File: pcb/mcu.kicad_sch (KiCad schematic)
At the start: 28 parts, among them J1 CON_SAMTEC_14P_2R_1m27_P_KEY_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, U3 IC_MCU_STM32F100C4T6B_48LQFP, X1 XTAL_8M_20PPM_18pF_ECS-80-18-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, X2 XTAL_32K768_10PPM_7pF_ECS-.32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

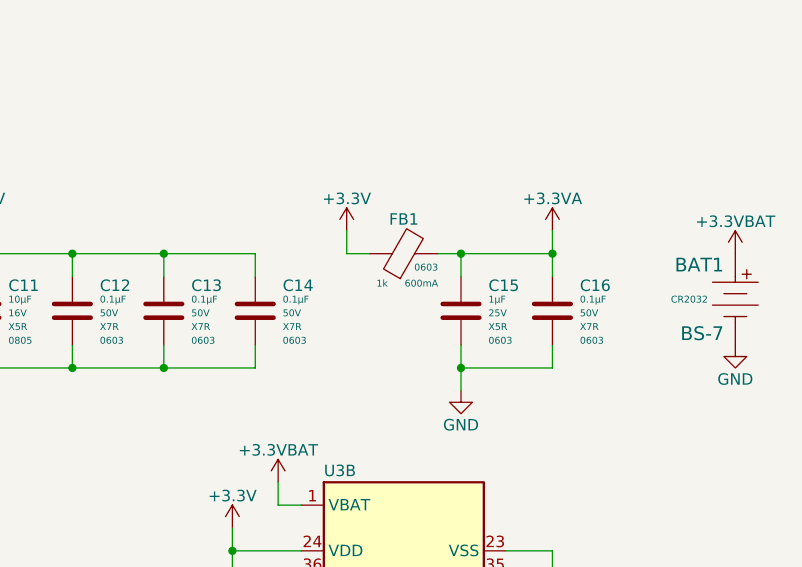
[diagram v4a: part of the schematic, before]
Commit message: Finished 12V boost circuit and updated sim to match
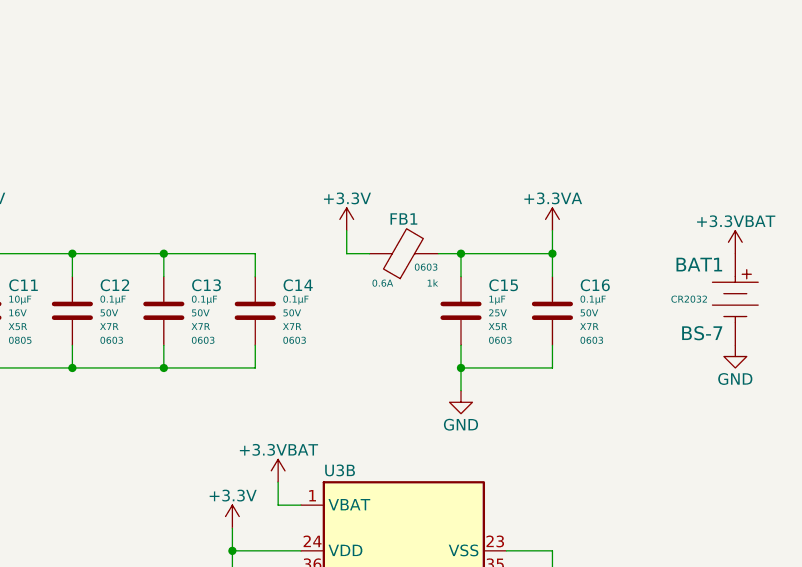
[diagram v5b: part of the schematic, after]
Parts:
- removed FB1: FER_1K_600mA_0603, Inductor_SMD:L_0603_1608Metric, symbol arjun_symbols:FER_1K_600mA_0603
- added FB1: FER_1K_0A6_0603, Inductor_SMD:L_0603_1608Metric, symbol .arjun:FER_1K_0A6_0603
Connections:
- net +3.3V: now also FB1.1
- net +3.3VA: now also FB1.2
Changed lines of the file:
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@@
+    (pin "2")
+  )
+  (symbol (lib_id ".arjun:FER_1K_0A6_0603") (at 233.68 104.14 0) (unit 1)
+    (in_bom yes) (on_board yes)
+    (property "Reference" "FB1" (id 0) (at 237.49 100.33 0))
+    (property "Value" "FER_1K_0A6_0603" (id 1) (at 263.525 97.79 0)
+      (effects (font (size 1.27 1.27)) hide)
+    )
+    (property "Footprint" "Inductor_SMD:L_0603_1608Metric" (id 2) (at 261.874 95.25 0)
+      (effects (font (size 1.27 1.27)) hide)
+    )
+    (property "Datasheet" "https://www.we-online.com/components/products/datasheet/742792662.pdf" (id 3) (at 291.465 110.49 0)
+      (effects (font (size 1.27 1.27)) hide)
+    )
+    (property "Manufacturer" "Würth Elektronik" (id 4) (at 253.365 100.33 0)
+      (effects (font (size 1.27 1.27)) (justify left) hide)
+    )
+    (property "ManufacturerPN" "742792662" (id 5) (at 253.365 102.87 0)
+      (effects (font (size 1.27 1.27)) (justify left) hide)
+    )
+    (property "Vendor" "Digi-Key" (id 6) (at 253.365 105.41 0)
+      (effects (font (size 1.27 1.27)) (justify left) hide)
+    )
+    (property "VendorPN" "732-4670-1-ND" (id 7) (at 253.365 107.95 0)
+      (effects (font (size 1.27 1.27)) (justify left) hide)
+    )
+    (property "Impedance@100MHz" "1k" (id 8) (at 241.3 107.442 0)
+      (effects (font (size 0.762 0.762)) (justify right))
+    )
+    (property "Rated Current" "0.6A" (id 9) (at 233.934 107.442 0)
+      (effects (font (size 0.762 0.762)) (justify left))
+    )
+    (property "Package" "0603" (id 10) (at 241.3 105.664 0)
+      (effects (font (size 0.762 0.762)) (justify right))
+    )
+    (pin "1")
     (pin "2")
   )
@@
     (pin "4")
   )
-  (symbol (lib_id "arjun_symbols:FER_1K_600mA_0603") (at 233.68 104.14 0) (unit 1)
-    (in_bom yes) (on_board yes)
-    (property "Reference" "FB1" (id 0) (at 237.49 100.33 0))
-    (property "Value" "FER_1K_600mA_0603" (id 1) (at 263.525 97.79 0)
-      (effects (font (size 1.27 1.27)) hide)
-    )
-    (property "Footprint" "Inductor_SMD:L_0603_1608Metric" (id 2) (at 261.874 95.25 0)
-      (effects (font (size 1.27 1.27)) hide)
-    )
-    (property "Datasheet" "https://www.we-online.com/components/products/datasheet/742792662.pdf" (id 3) (at 291.465 110.49 0)
-      (effects (font (size 1.27 1.27)) hide)
-    )
-    (property "Manufacturer" "Würth Elektronik" (id 4) (at 253.365 100.33 0)
-      (effects (font (size 1.27 1.27)) (justify left) hide)
-    )
-    (property "ManufacturerPN" "742792662" (id 5) (at 253.365 102.87 0)
-      (effects (font (size 1.27 1.27)) (justify left) hide)
-    )
-    (property "Vendor" "Digi-Key" (id 6) (at 253.365 105.41 0)
-      (effects (font (size 1.27 1.27)) (justify left) hide)
-    )
-    (property "VendorPN" "732-4670-1-ND" (id 7) (at 253.365 107.95 0)
-      (effects (font (size 1.27 1.27)) (justify left) hide)
-    )
-    (property "Impedance@100MHz" "1k" (id 8) (at 234.442 107.442 0)
-      (effects (font (size 0.762 0.762)) (justify left))
-    )
-    (property "Rated Current" "600mA" (id 9) (at 241.3 107.442 0)
-      (effects (font (size 0.762 0.762)) (justify right))
-    )
-    (property "Package" "0603" (id 10) (at 241.3 105.664 0)
-      (effects (font (size 0.762 0.762)) (justify right))
-    )
-    (pin "1")
-    (pin "2")
-  )
   (symbol (lib_id "power:+3.3V") (at 218.44 134.62 0) (unit 1)

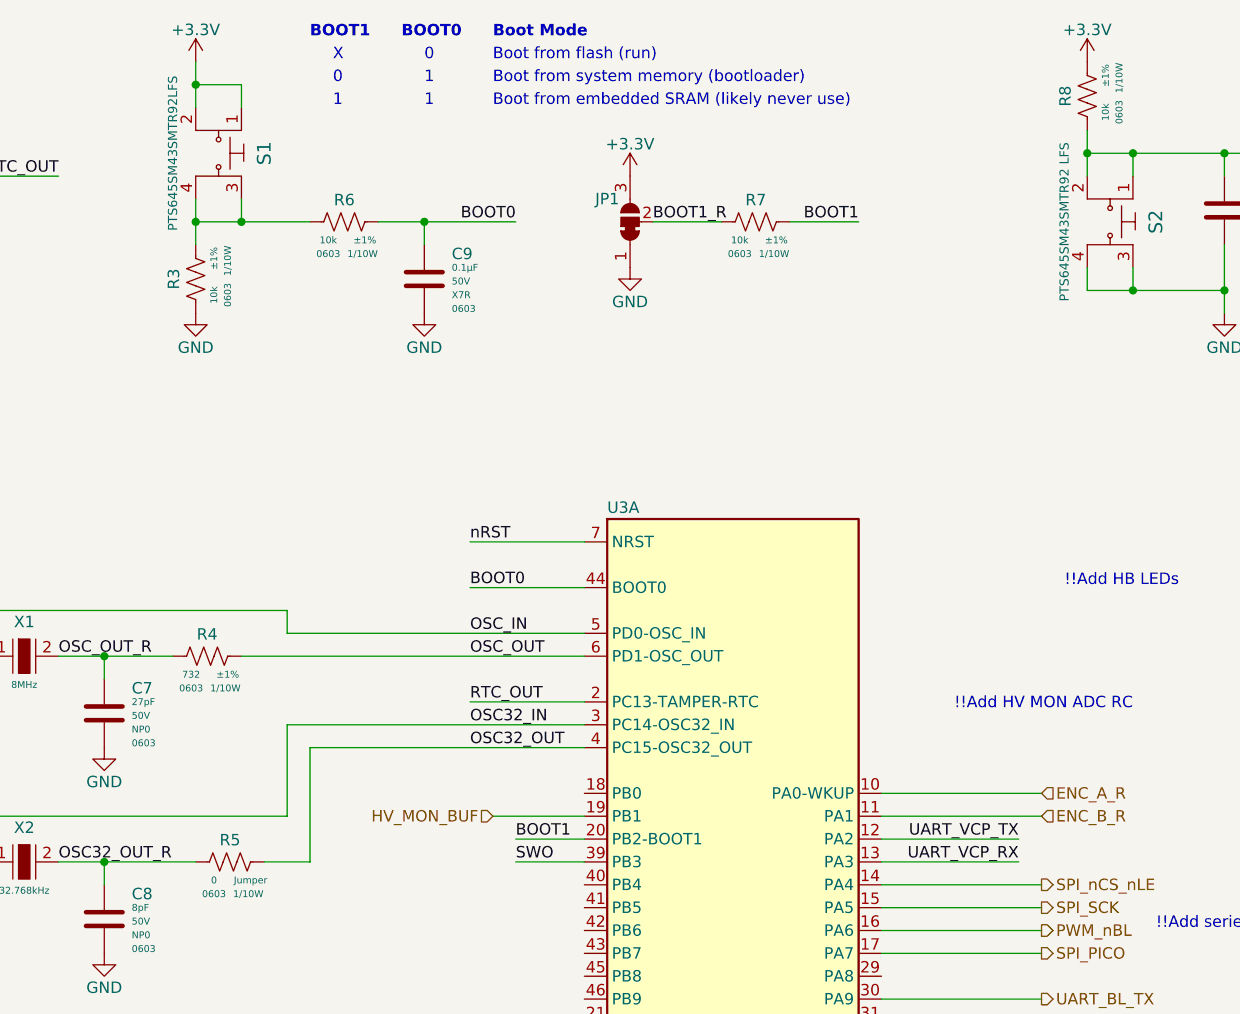
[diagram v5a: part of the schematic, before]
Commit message: Added snubber DNP footprints and named nets on power page.
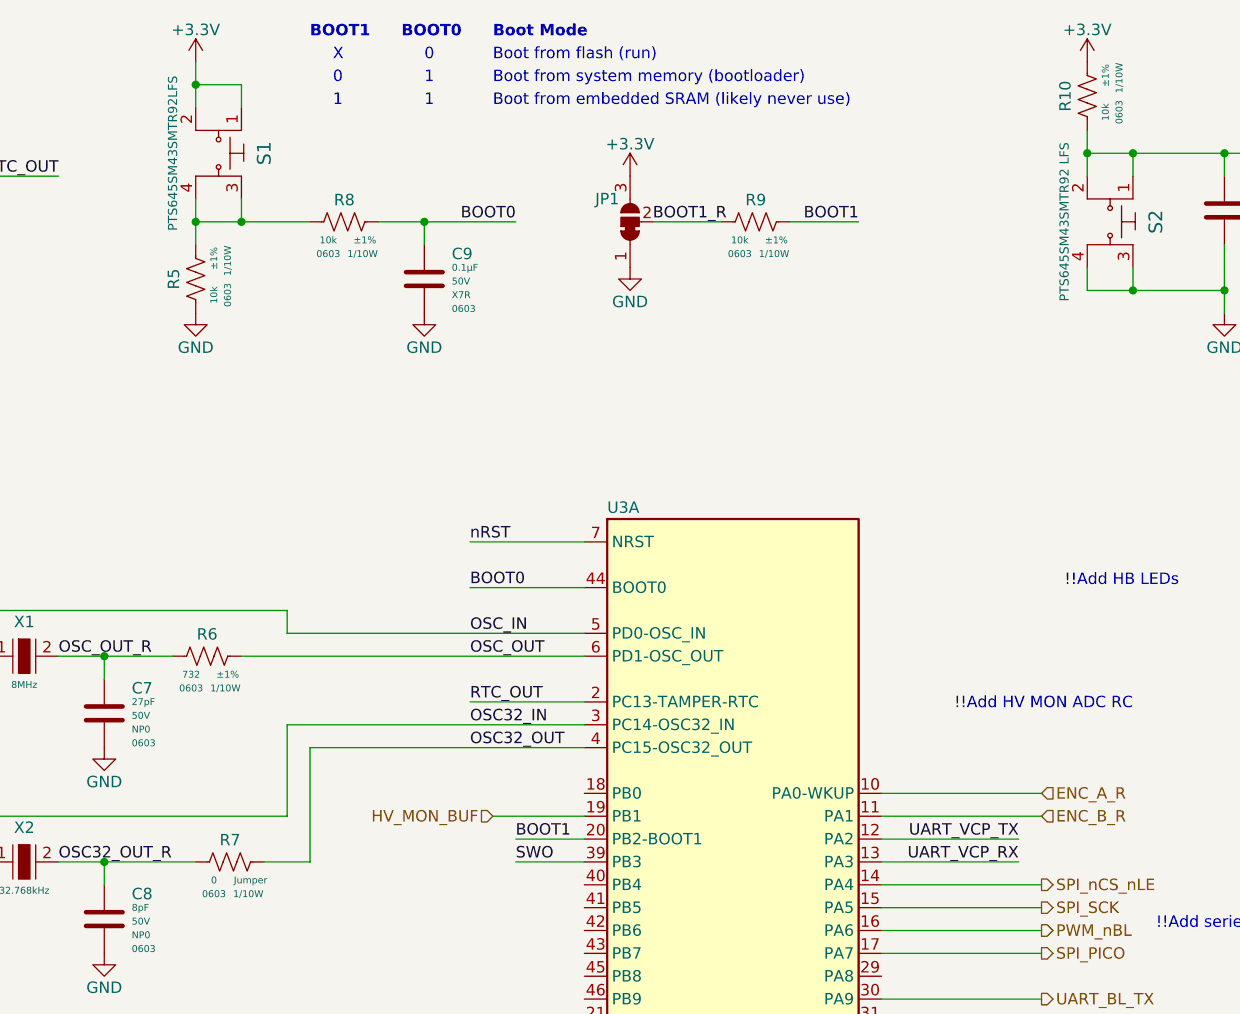
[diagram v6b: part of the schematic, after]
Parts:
- renumbered R8 to R10, R3 to R5, R4 to R6, R5 to R7, R6 to R8, R7 to R9
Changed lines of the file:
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@@
   (symbol (lib_id "power:GND") (at 243.84 119.38 0) (unit 1)
     (in_bom yes) (on_board yes)
-    (property "Reference" "#PWR026" (id 0) (at 243.84 125.73 0)
+    (property "Reference" "#PWR027" (id 0) (at 243.84 125.73 0)
       (effects (font (size 1.27 1.27)) hide)
     )
@@
   (symbol (lib_id "power:GND") (at 48.26 106.68 0) (unit 1)
     (in_bom yes) (on_board yes)
-    (property "Reference" "#PWR011" (id 0) (at 48.26 113.03 0)
+    (property "Reference" "#PWR012" (id 0) (at 48.26 113.03 0)
       (effects (font (size 1.27 1.27)) hide)
     )
@@
   (symbol (lib_id "arjun_symbols:+3.3VBAT") (at 274.32 104.14 0) (unit 1)
     (in_bom yes) (on_board yes)
-    (property "Reference" "#PWR029" (id 0) (at 274.32 107.95 0)
+    (property "Reference" "#PWR030" (id 0) (at 274.32 107.95 0)
       (effects (font (size 1.27 1.27)) hide)
     )
@@
   (symbol (lib_id "power:GND") (at 27.94 129.54 0) (unit 1)
     (in_bom yes) (on_board yes)
-    (property "Reference" "#PWR08" (id 0) (at 27.94 135.89 0)
+    (property "Reference" "#PWR09" (id 0) (at 27.94 135.89 0)
       (effects (font (size 1.27 1.27)) hide)
     )
@@
   (symbol (lib_id "power:GND") (at 58.42 58.42 0) (unit 1)
     (in_bom yes) (on_board yes)
-    (property "Reference" "#PWR014" (id 0) (at 58.42 64.77 0)
+    (property "Reference" "#PWR015" (id 0) (at 58.42 64.77 0)
       (effects (font (size 1.27 1.27)) hide)
     )
@@
   (symbol (lib_id "arjun_symbols:RES_10K_1P_1{slash}10W_0603") (at 78.74 48.26 270) (unit 1)
     (in_bom yes) (on_board yes)
-    (property "Reference" "R6" (id 0) (at 74.93 45.085 90)
+    (property "Reference" "R8" (id 0) (at 74.93 45.085 90)
       (effects (font (size 1.27 1.27)) (justify top))
     )
@@
   (symbol (lib_id "power:GND") (at 48.26 129.54 0) (unit 1)
     (in_bom yes) (on_board yes)
-    (property "Reference" "#PWR012" (id 0) (at 48.26 135.89 0)
+    (property "Reference" "#PWR013" (id 0) (at 48.26 135.89 0)
       (effects (font (size 1.27 1.27)) hide)
     )
@@
   (symbol (lib_id "arjun_symbols:RES_10K_1P_1{slash}10W_0603") (at 124.46 48.26 270) (unit 1)
     (in_bom yes) (on_board yes)
-    (property "Reference" "R7" (id 0) (at 120.65 45.085 90)
+    (property "Reference" "R9" (id 0) (at 120.65 45.085 90)
       (effects (font (size 1.27 1.27)) (justify top))
     )
@@
   (symbol (lib_id "power:+3.3V") (at 157.48 30.48 0) (unit 1)
     (in_bom yes) (on_board yes)
-    (property "Reference" "#PWR018" (id 0) (at 157.48 34.29 0)
+    (property "Reference" "#PWR019" (id 0) (at 157.48 34.29 0)
       (effects (font (size 1.27 1.27)) hide)
     )
@@
   (symbol (lib_id "power:GND") (at 172.72 58.42 0) (unit 1)
     (in_bom yes) (on_board yes)
-    (property "Reference" "#PWR019" (id 0) (at 172.72 64.77 0)
+    (property "Reference" "#PWR020" (id 0) (at 172.72 64.77 0)
       (effects (font (size 1.27 1.27)) hide)
     )
@@
   (symbol (lib_id "power:GND") (at 190.5 119.38 0) (unit 1)
     (in_bom yes) (on_board yes)
-    (property "Reference" "#PWR021" (id 0) (at 190.5 125.73 0)
+    (property "Reference" "#PWR022" (id 0) (at 190.5 125.73 0)
       (effects (font (size 1.27 1.27)) hide)
     )
@@
   (symbol (lib_id "power:GND") (at 274.32 114.3 0) (unit 1)
     (in_bom yes) (on_board yes)
-    (property "Reference" "#PWR030" (id 0) (at 274.32 120.65 0)
+    (property "Reference" "#PWR031" (id 0) (at 274.32 120.65 0)
       (effects (font (size 1.27 1.27)) hide)
     )
@@
   (symbol (lib_id "arjun_symbols:RES_10K_1P_1{slash}10W_0603") (at 58.42 50.8 0) (unit 1)
     (in_bom yes) (on_board yes)
-    (property "Reference" "R3" (id 0) (at 55.245 54.61 90)
+    (property "Reference" "R5" (id 0) (at 55.245 54.61 90)
       (effects (font (size 1.27 1.27)) (justify top))
     )
@@
   (symbol (lib_id "arjun_symbols:RES_10K_1P_1{slash}10W_0603") (at 157.48 30.48 0) (unit 1)
     (in_bom yes) (on_board yes)
-    (property "Reference" "R8" (id 0) (at 154.305 34.29 90)
+    (property "Reference" "R10" (id 0) (at 154.305 34.29 90)
       (effects (font (size 1.27 1.27)) (justify top))
     )
@@
   (symbol (lib_id "power:+3.3V") (at 190.5 101.6 0) (unit 1)
     (in_bom yes) (on_board yes)
-    (property "Reference" "#PWR020" (id 0) (at 190.5 105.41 0)
+    (property "Reference" "#PWR021" (id 0) (at 190.5 105.41 0)
       (effects (font (size 1.27 1.27)) hide)
     )
@@
   (symbol (lib_id "power:GND") (at 83.82 58.42 0) (unit 1)
     (in_bom yes) (on_board yes)
-    (property "Reference" "#PWR015" (id 0) (at 83.82 64.77 0)
+    (property "Reference" "#PWR016" (id 0) (at 83.82 64.77 0)
       (effects (font (size 1.27 1.27)) hide)
     )
@@
   (symbol (lib_id "power:+3.3V") (at 106.68 43.18 0) (unit 1)
     (in_bom yes) (on_board yes)
-    (property "Reference" "#PWR016" (id 0) (at 106.68 46.99 0)
+    (property "Reference" "#PWR017" (id 0) (at 106.68 46.99 0)
       (effects (font (size 1.27 1.27)) hide)
     )
@@
   (symbol (lib_id "arjun_symbols:RES_732R_1P_1{slash}10W_0603") (at 63.5 96.52 270) (unit 1)
     (in_bom yes) (on_board yes)
-    (property "Reference" "R4" (id 0) (at 59.69 93.345 90)
+    (property "Reference" "R6" (id 0) (at 59.69 93.345 90)
       (effects (font (size 1.27 1.27)) (justify top))
     )
@@
   (symbol (lib_id "power:+3.3V") (at 231.14 101.6 0) (unit 1)
     (in_bom yes) (on_board yes)
-    (property "Reference" "#PWR025" (id 0) (at 231.14 105.41 0)
+    (property "Reference" "#PWR026" (id 0) (at 231.14 105.41 0)
       (effects (font (size 1.27 1.27)) hide)
     )
@@
   (symbol (lib_id "power:+3.3VA") (at 254 101.6 0) (unit 1)
     (in_bom yes) (on_board yes)
-    (property "Reference" "#PWR027" (id 0) (at 254 105.41 0)
+    (property "Reference" "#PWR028" (id 0) (at 254 105.41 0)
       (effects (font (size 1.27 1.27)) hide)
     )
@@
   (symbol (lib_id "power:+3.3V") (at 38.1 160.02 0) (unit 1)
     (in_bom yes) (on_board yes)
-    (property "Reference" "#PWR010" (id 0) (at 38.1 163.83 0)
+    (property "Reference" "#PWR011" (id 0) (at 38.1 163.83 0)
       (effects (font (size 1.27 1.27)) hide)
     )
@@
   (symbol (lib_id "power:+3.3VA") (at 213.36 144.78 0) (unit 1)
     (in_bom yes) (on_board yes)
-    (property "Reference" "#PWR022" (id 0) (at 213.36 148.59 0)
+    (property "Reference" "#PWR023" (id 0) (at 213.36 148.59 0)
       (effects (font (size 1.27 1.27)) hide)
     )
@@
   (symbol (lib_id "arjun_symbols:+3.3VBAT") (at 223.52 129.54 0) (unit 1)
     (in_bom yes) (on_board yes)
-    (property "Reference" "#PWR024" (id 0) (at 223.52 133.35 0)
+    (property "Reference" "#PWR025" (id 0) (at 223.52 133.35 0)
       (effects (font (size 1.27 1.27)) hide)
     )
@@
   (symbol (lib_id "power:GND") (at 27.94 177.8 0) (unit 1)
     (in_bom yes) (on_board yes)
-    (property "Reference" "#PWR09" (id 0) (at 27.94 184.15 0)
+    (property "Reference" "#PWR010" (id 0) (at 27.94 184.15 0)
       (effects (font (size 1.27 1.27)) hide)
     )
@@
   (symbol (lib_id "power:GND") (at 254 149.86 0) (unit 1)
     (in_bom yes) (on_board yes)
-    (property "Reference" "#PWR028" (id 0) (at 254 156.21 0)
+    (property "Reference" "#PWR029" (id 0) (at 254 156.21 0)
       (effects (font (size 1.27 1.27)) hide)
     )
@@
   (symbol (lib_id "arjun_symbols:RES_0R_1{slash}10W_0603") (at 66.04 119.38 270) (unit 1)
     (in_bom yes) (on_board yes)
-    (property "Reference" "R5" (id 0) (at 62.23 116.205 90)
+    (property "Reference" "R7" (id 0) (at 62.23 116.205 90)
       (effects (font (size 1.27 1.27)) (justify top))
     )
@@
   (symbol (lib_id "power:GND") (at 106.68 53.34 0) (unit 1)
     (in_bom yes) (on_board yes)
-    (property "Reference" "#PWR017" (id 0) (at 106.68 59.69 0)
+    (property "Reference" "#PWR018" (id 0) (at 106.68 59.69 0)
       (effects (font (size 1.27 1.27)) hide)
     )
@@
   (symbol (lib_id "power:+3.3V") (at 58.42 30.48 0) (unit 1)
     (in_bom yes) (on_board yes)
-    (property "Reference" "#PWR013" (id 0) (at 58.42 34.29 0)
+    (property "Reference" "#PWR014" (id 0) (at 58.42 34.29 0)
       (effects (font (size 1.27 1.27)) hide)
     )
@@
   (symbol (lib_id "power:+3.3V") (at 218.44 134.62 0) (unit 1)
     (in_bom yes) (on_board yes)
-    (property "Reference" "#PWR023" (id 0) (at 218.44 138.43 0)
+    (property "Reference" "#PWR024" (id 0) (at 218.44 138.43 0)
       (effects (font (size 1.27 1.27)) hide)
     )
@@
   (symbol (lib_id "power:GND") (at 27.94 106.68 0) (unit 1)
     (in_bom yes) (on_board yes)
-    (property "Reference" "#PWR07" (id 0) (at 27.94 113.03 0)
-      (effects (font (size 1.27 1.27)) hide)
-    )
+    (property "Reference" "#PWR08" (id 0) (at 27.94 113.03 0)
+      (effects (font (size 1.27 1.27)) hide)
+    )
